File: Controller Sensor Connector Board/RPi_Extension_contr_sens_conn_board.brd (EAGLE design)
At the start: 100 x 100 mm, 39 parts, among them J1 22-27-2051-05, J2 22-27-2051-05, X17 53047-03, X18 53047-03, X19 53047-03, X20 53047-03, X21 53047-03, X22 53047-03, X23 53047-03, X24 53047-03, X25 53047-03, X26 53047-03, X27 53047-03, X28 53047-03, X29 53047-03, X30 53047-03, X31 53047-03, X32 53047-03

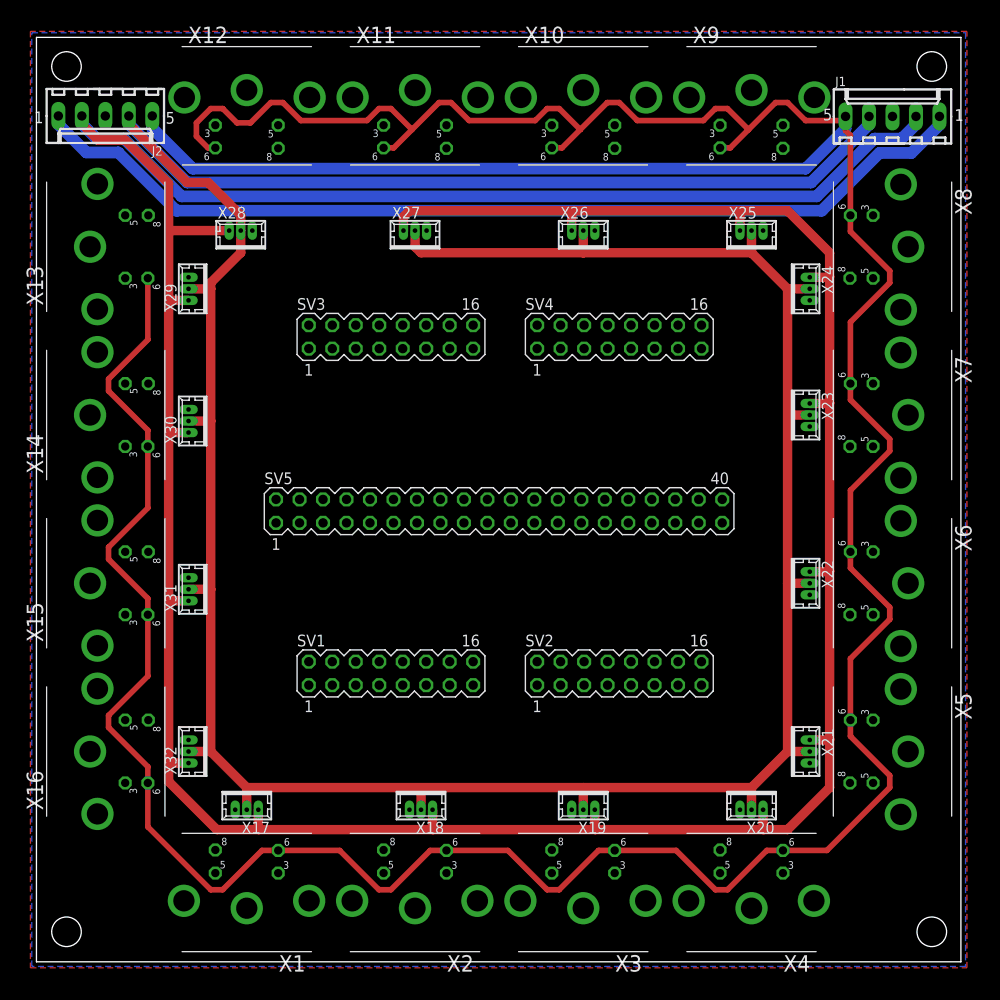
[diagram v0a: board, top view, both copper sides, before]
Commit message: added 40pin connector using 3pin 2row for each muscle
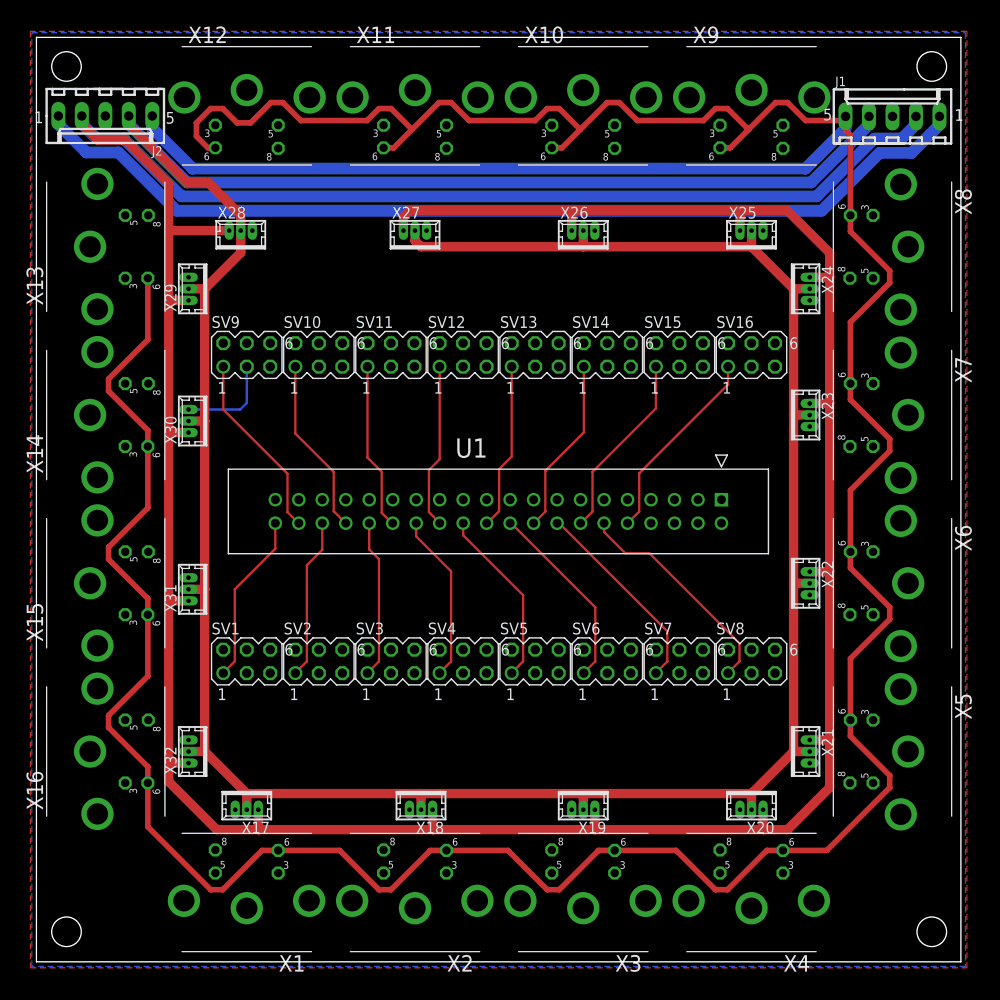
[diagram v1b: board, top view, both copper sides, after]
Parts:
- added SV10, SV11, SV12, SV13, SV14, SV15, SV16, SV6, SV7, SV8, SV9: (no value), con-lstb:MA03-2
- added U1: 5103309-8, AMP 5103309-8 40pin:TYCO_5103309-8
- SV1, SV2, SV3, SV4: device con-lstb:MA08-2 -> con-lstb:MA03-2
- SV5: device con-lstb:MA20-2 -> con-lstb:MA03-2
- moved SV4 39.0 mm to (46.1, 32.5)
- moved SV3 35.1 mm to (38.4, 32.5)
- moved SV2 32.5 mm to (30.6, 32.5)
- moved SV5 16.7 mm to (54.0, 32.5)
- moved SV1 15.7 mm to (22.8, 32.5)
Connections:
- removed net N$43: X30.1
- new net ADC_1: SV1.3
- new net ADC_10: SV10.3
- new net ADC_11: SV11.3
- new net ADC_12: SV12.3
- new net ADC_13: SV13.3
- new net ADC_14: SV14.3
- new net ADC_15: SV15.3
- new net ADC_16: SV16.3
- new net ADC_2: SV2.3
- new net ADC_3: SV3.3
- new net ADC_4: SV4.3
- new net ADC_5: SV5.3
- new net ADC_6: SV6.3
- new net ADC_7: SV7.3
- new net ADC_8: SV8.3
- new net ADC_9: SV9.3, X30.1
- new net DAC_1: SV1.1, U1.40
- new net DAC_10: SV10.1, U1.34
- new net DAC_11: SV11.1, U1.30
- new net DAC_12: SV12.1, U1.26
- new net DAC_13: SV13.1, U1.22
- new net DAC_14: SV14.1, U1.18
- new net DAC_15: SV15.1, U1.14
- new net DAC_16: SV16.1, U1.10
- new net DAC_2: SV2.1, U1.36
- new net DAC_3: SV3.1, U1.32
- new net DAC_4: SV4.1, U1.28
- new net DAC_5: SV5.1, U1.24
- new net DAC_6: SV6.1, U1.20
- new net DAC_7: SV7.1, U1.16
- new net DAC_8: SV8.1, U1.12
- new net DAC_9: SV9.1, U1.38
- new net N$100: X1.5
- new net N$101: X5.3
- new net N$102: X5.5
- new net N$103: X9.5
- new net N$104: X9.3
- new net N$105: X2.5
- new net N$106: X2.3
- new net N$107: X6.5
- new net N$108: X6.3
- new net N$109: X10.5
- new net N$11: X11.3
- new net N$110: X10.3
- new net N$111: X16.5
- new net N$112: X16.3
- new net N$12: X11.5
- new net N$14: X7.3
- new net N$15: X7.5
- new net N$17: X3.3
- new net N$18: X3.5
- new net N$2: X13.5
- new net N$20: X4.3
- new net N$21: X4.5
- new net N$23: X8.5
- new net N$24: X8.3
- new net N$26: X12.5
- new net N$27: X12.3
- new net N$3: X13.3
- new net N$5: X14.5
- new net N$6: X14.3
- new net N$67: SV1.6
- new net N$68: SV1.5
- new net N$69: SV5.5
- new net N$70: SV5.6
- new net N$71: SV2.6
- new net N$72: SV2.5
- new net N$73: SV6.6
- new net N$74: SV6.5
- new net N$75: SV9.6
- new net N$76: SV9.5
- new net N$77: SV13.6
- new net N$78: SV13.5
- new net N$79: SV10.6
- new net N$8: X15.3
- new net N$80: SV10.5
- new net N$81: SV14.5
- new net N$82: SV14.6
- new net N$83: SV15.5
- new net N$84: SV15.6
- new net N$85: SV16.6
- new net N$86: SV16.5
- new net N$87: SV12.5
- new net N$88: SV12.6
- new net N$89: SV11.6
- new net N$9: X15.5
- new net N$90: SV11.5
- new net N$91: SV8.5
- new net N$92: SV8.6
- new net N$93: SV4.5
- new net N$94: SV4.6
- new net N$95: SV3.5
- new net N$96: SV3.6
- new net N$97: SV7.5
- new net N$98: SV7.6
- new net N$99: X1.3
- net GND: now also SV1.2, SV1.4, SV10.2, SV10.4, SV11.2, SV11.4, SV12.2, SV12.4, SV13.2, SV13.4, SV14.2, SV14.4, SV15.2, SV15.4, SV16.2, SV16.4, SV2.2, SV2.4, SV3.2, SV3.4, SV4.2, SV4.4, SV5.2, SV5.4, SV6.2, SV6.4, SV7.2, SV7.4, SV8.2, SV8.4, SV9.2, SV9.4, U1.1, U1.11, U1.13, U1.15, U1.17, U1.19, U1.21, U1.23, U1.25, U1.27, U1.29, U1.3, U1.31, U1.33, U1.35, U1.37, U1.39, U1.5, U1.7, U1.9
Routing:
- net DAC_8: track 0.00 -> 24.3 mm
- net DAC_7: track 0.00 -> 21.8 mm
- net DAC_16: track 0.00 -> 21.4 mm
- net DAC_6: track 0.00 -> 20.6 mm
- net DAC_9: track 0.00 -> 20.3 mm
- net DAC_15: track 0.00 -> 20.3 mm
- net DAC_5: track 0.00 -> 19.4 mm
- net DAC_10: track 0.00 -> 19.2 mm
- net DAC_14: track 0.00 -> 19.2 mm
- net DAC_1: track 0.00 -> 18.6 mm
- net DAC_4: track 0.00 -> 18.3 mm
- net DAC_11: track 0.00 -> 18.1 mm
- net DAC_13: track 0.00 -> 18.1 mm
- net DAC_12: track 0.00 -> 17.9 mm
- net DAC_2: track 0.00 -> 17.4 mm
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
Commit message: finished first half of connector board
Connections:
- net N$67 renamed LC_P_1
- net N$68 renamed LC_N_1
- removed net N$103: X9.5
- removed net N$104: X9.3
- removed net N$109: X10.5
- removed net N$11: X11.3
- removed net N$110: X10.3
- removed net N$12: X11.5
- removed net N$13: X24.1
- removed net N$14: X7.3
- removed net N$15: X7.5
- removed net N$16: X23.1
- removed net N$2: X13.5
- removed net N$23: X8.5
- removed net N$24: X8.3
- removed net N$25: X25.1
- removed net N$26: X12.5
- removed net N$27: X12.3
- removed net N$28: X26.1
- removed net N$3: X13.3
- removed net N$31: X27.1
- removed net N$34: X28.1
- removed net N$46: X29.1
- removed net N$5: X14.5
- removed net N$6: X14.3
- removed net N$75: SV9.6
- removed net N$76: SV9.5
- removed net N$77: SV13.6
- removed net N$78: SV13.5
- removed net N$79: SV10.6
- removed net N$80: SV10.5
- removed net N$81: SV14.5
- removed net N$82: SV14.6
- removed net N$83: SV15.5
- removed net N$84: SV15.6
- removed net N$85: SV16.6
- removed net N$86: SV16.5
- removed net N$87: SV12.5
- removed net N$88: SV12.6
- removed net N$89: SV11.6
- removed net N$90: SV11.5
- new net LC_N_10: SV10.5, X13.3
- new net LC_N_11: SV11.5, X12.3
- new net LC_N_12: SV12.5, X11.3
- new net LC_N_13: SV13.5, X10.3
- new net LC_N_14: SV14.5, X9.3
- new net LC_N_15: SV15.5, X8.3
- new net LC_N_16: SV16.5, X7.3
- new net LC_N_9: SV9.5, X14.3
- new net LC_P_10: SV10.6, X13.5
- new net LC_P_11: SV11.6, X12.5
- new net LC_P_12: SV12.6, X11.5
- new net LC_P_13: SV13.6, X10.5
- new net LC_P_14: SV14.6, X9.5
- new net LC_P_15: SV15.6, X8.5
- new net LC_P_16: SV16.6, X7.5
- new net LC_P_9: SV9.6, X14.5
- net ADC_10: now also X29.1
- net ADC_11: now also X28.1
- net ADC_12: now also X27.1
- net ADC_13: now also X26.1
- net ADC_14: now also X25.1
- net ADC_15: now also X24.1
- net ADC_16: now also X23.1
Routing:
- net LC_P_14: track 0.00 -> 92.1 mm
- net LC_N_14: track 0.00 -> 88.8 mm
- net LC_P_13: track 0.00 -> 69.2 mm
- net LC_N_13: track 0.00 -> 66.9 mm
- net LC_P_12: track 0.00 -> 46.3 mm
- net LC_N_12: track 0.00 -> 42.8 mm
- net LC_N_11: track 0.00 -> 37.3 mm
- net LC_P_9: track 0.00 -> 36.1 mm
- net LC_P_11: track 0.00 -> 33.6 mm
- net LC_N_15: track 0.00 -> 33.5 mm
- net LC_P_10: track 0.00 -> 31.6 mm
- net LC_N_10: track 0.00 -> 29.8 mm
- net ADC_14: track 0.00 -> 25.5 mm
- net ADC_11: track 0.00 -> 22.6 mm
- net LC_P_15: track 0.00 -> 22.3 mm
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
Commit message: finished second half of connector board
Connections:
- removed net N$1: X17.1
- removed net N$10: X20.1
- removed net N$100: X1.5
- removed net N$101: X5.3
- removed net N$102: X5.5
- removed net N$105: X2.5
- removed net N$106: X2.3
- removed net N$107: X6.5
- removed net N$108: X6.3
- removed net N$111: X16.5
- removed net N$112: X16.3
- removed net N$17: X3.3
- removed net N$18: X3.5
- removed net N$19: X22.1
- removed net N$20: X4.3
- removed net N$21: X4.5
- removed net N$22: X21.1
- removed net N$37: X32.1
- removed net N$4: X18.1
- removed net N$40: X31.1
- removed net N$69: SV5.5
- removed net N$7: X19.1
- removed net N$70: SV5.6
- removed net N$71: SV2.6
- removed net N$72: SV2.5
- removed net N$73: SV6.6
- removed net N$74: SV6.5
- removed net N$8: X15.3
- removed net N$9: X15.5
- removed net N$91: SV8.5
- removed net N$92: SV8.6
- removed net N$93: SV4.5
- removed net N$94: SV4.6
- removed net N$95: SV3.5
- removed net N$96: SV3.6
- removed net N$97: SV7.5
- removed net N$98: SV7.6
- removed net N$99: X1.3
- new net LC_N_2: SV2.5, X16.3
- new net LC_N_3: SV3.5, X1.3
- new net LC_N_4: SV4.5, X2.3
- new net LC_N_5: SV5.5, X3.3
- new net LC_N_6: SV6.5, X4.3
- new net LC_N_7: SV7.5, X5.3
- new net LC_N_8: SV8.5, X6.3
- new net LC_P_2: SV2.6, X16.5
- new net LC_P_3: SV3.6, X1.5
- new net LC_P_4: SV4.6, X2.5
- new net LC_P_5: SV5.6, X3.5
- new net LC_P_6: SV6.6, X4.5
- new net LC_P_7: SV7.6, X5.5
- new net LC_P_8: SV8.6, X6.5
- net ADC_1: now also X31.1
- net ADC_2: now also X32.1
- net ADC_3: now also X17.1
- net ADC_4: now also X18.1
- net ADC_5: now also X19.1
- net ADC_6: now also X20.1
- net ADC_7: now also X21.1
- net ADC_8: now also X22.1
- net LC_N_1: now also X15.3
- net LC_P_1: now also X15.5
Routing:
- net LC_P_6: track 0.00 -> 39.3 mm
- net LC_P_2: track 0.00 -> 35.9 mm
- net LC_P_3: track 0.00 -> 33.9 mm
- net LC_N_6: track 0.00 -> 33.7 mm
- net LC_P_5: track 0.00 -> 32.1 mm
- net LC_N_2: track 0.00 -> 31.1 mm
- net LC_P_4: track 0.00 -> 29.9 mm
- net LC_P_7: track 0.00 -> 29.5 mm
- net LC_P_1: track 0.00 -> 28.4 mm
- net LC_N_3: track 0.00 -> 27.8 mm
- net LC_N_5: track 0.00 -> 25.8 mm
- net ADC_3: track 0.00 -> 25.6 mm
- net LC_N_4: track 0.00 -> 23.4 mm
- net ADC_6: track 0.00 -> 22.8 mm
- net LC_N_8: track 0.00 -> 22.7 mm
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
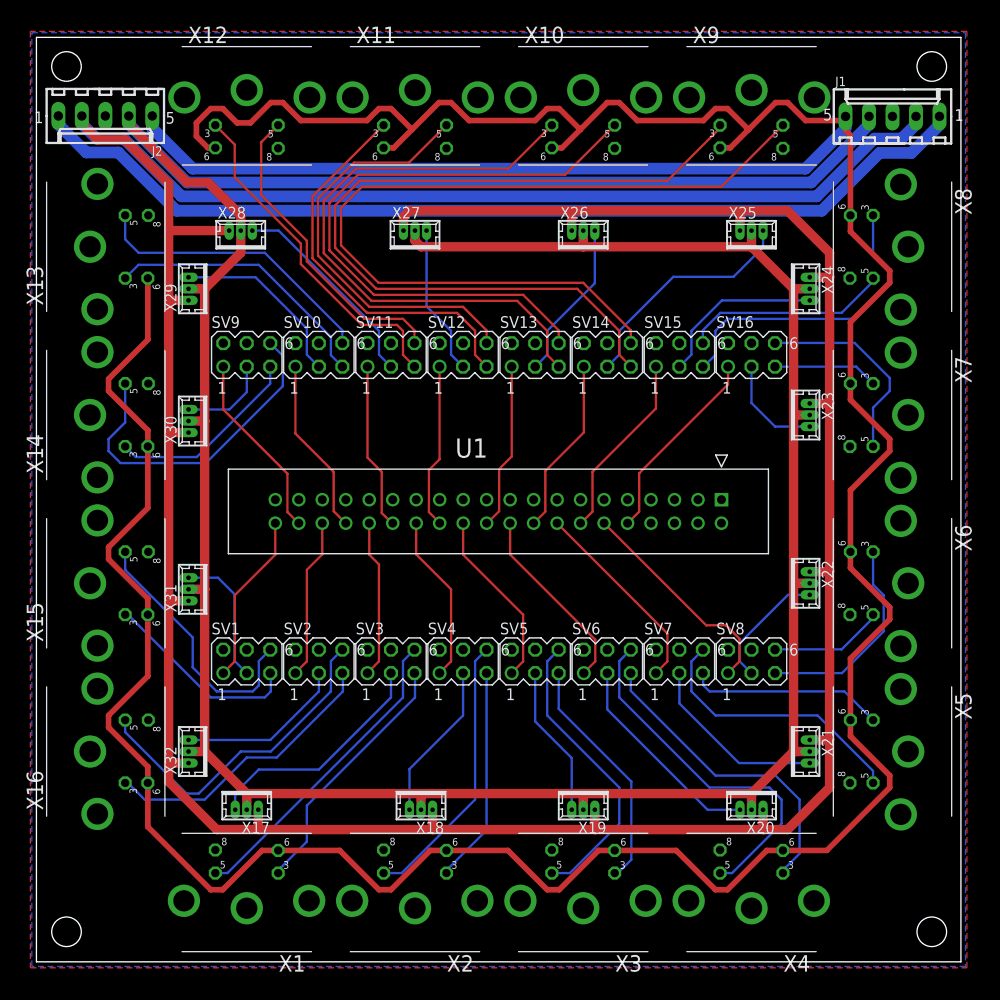
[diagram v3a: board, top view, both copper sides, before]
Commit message: adjusted silkscreen
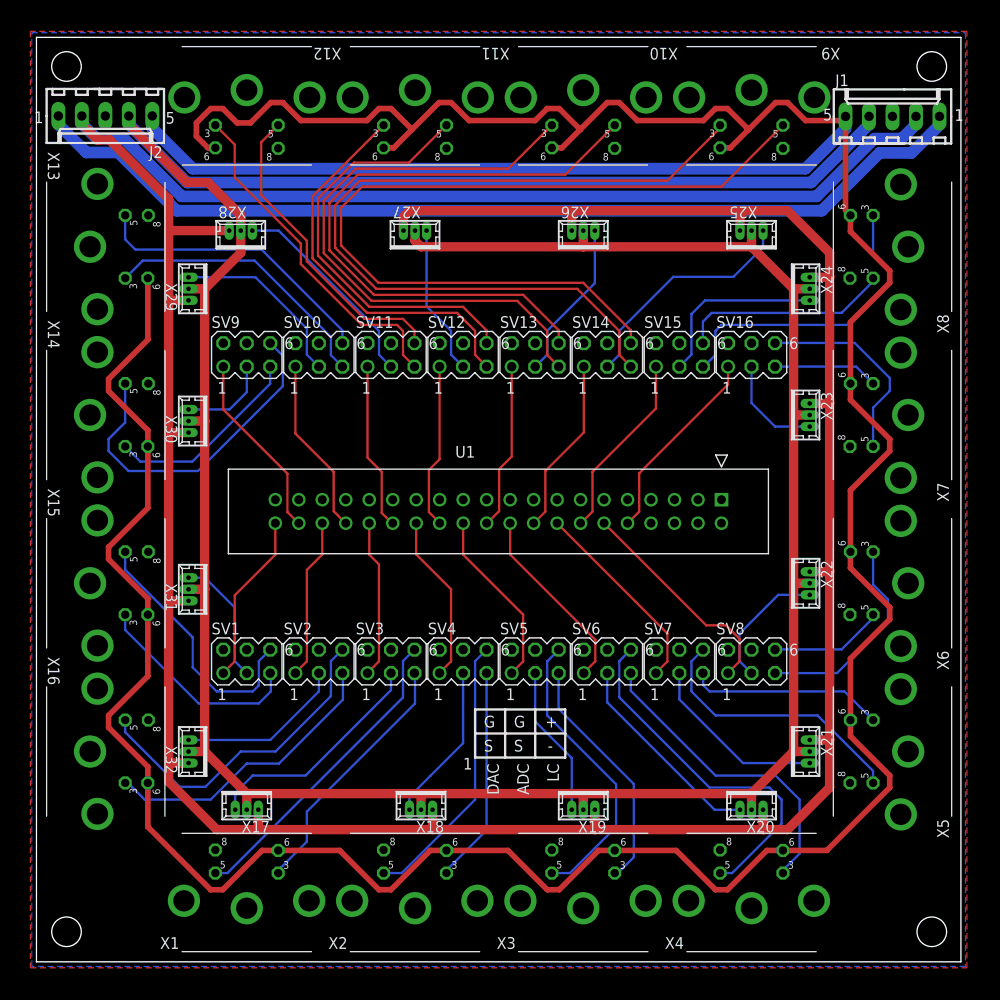
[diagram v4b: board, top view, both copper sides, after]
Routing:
- net LC_N_1: track 21.7 -> 23.2 mm
- net ADC_15: track 18.6 -> 19.6 mm
- net +12V: track 396.2 -> 395.2 mm
- net ADC_1: track 14.8 -> 14.0 mm
- net LC_P_9: track 36.1 -> 36.8 mm
- net ADC_8: track 13.5 -> 14.1 mm
- net LC_P_15: track 22.3 -> 22.9 mm
- net LC_N_2: track 31.1 -> 31.7 mm
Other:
- board text added: "+"
- board text added: "-"
- board text added: "1"
- board text added: "ADC"
- board text added: "DAC"
- board text added: "G"
- board text added: "LC"
- board text added: "S"

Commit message: changed dac header to 34pin
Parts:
- U1: value 5103309-8 -> 5103309-7; device AMP 5103309-8 40pin:TYCO_5103309-8 -> AMP 5103309-7 34pin:TYCO_5103309-7
- moved U1 43.7 mm to (30.6, 50.7), turned to 180 degrees
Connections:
- net DAC_1: now also U1.1; no longer U1.40
- net DAC_10: now also U1.7; no longer U1.34
- net DAC_11: now also U1.11; no longer U1.30
- net DAC_12: now also U1.15; no longer U1.26
- net DAC_13: now also U1.19; no longer U1.22
- net DAC_14: now also U1.23; no longer U1.18
- net DAC_15: now also U1.27; no longer U1.14
- net DAC_16: now also U1.31; no longer U1.10
- net DAC_2: now also U1.5; no longer U1.36
- net DAC_3: now also U1.9; no longer U1.32
- net DAC_4: now also U1.13; no longer U1.28
- net DAC_5: now also U1.17; no longer U1.24
- net DAC_6: now also U1.21; no longer U1.20
- net DAC_7: now also U1.25; no longer U1.16
- net DAC_8: now also U1.29; no longer U1.12
- net DAC_9: now also U1.3; no longer U1.38
- net GND: now also U1.10, U1.12, U1.14, U1.16, U1.18, U1.2, U1.20, U1.22, U1.24, U1.26, U1.28, U1.30, U1.32, U1.34, U1.4, U1.6, U1.8; no longer U1.1, U1.11, U1.13, U1.15, U1.17, U1.19, U1.21, U1.23, U1.25, U1.27, U1.29, U1.3, U1.31, U1.33, U1.35, U1.37, U1.39, U1.5, U1.7, U1.9
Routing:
- net DAC_15: track 20.3 -> 17.6 mm
- net DAC_16: track 21.4 -> 18.8 mm
- net DAC_2: track 17.4 -> 20.1 mm
- net DAC_1: track 18.6 -> 21.2 mm
- net DAC_8: track 24.1 -> 21.6 mm
- net DAC_3: track 17.2 -> 19.0 mm
- net DAC_14: track 19.2 -> 17.6 mm
- net DAC_7: track 21.7 -> 20.4 mm
- net DAC_6: track 20.5 -> 19.3 mm
- net DAC_5: track 19.4 -> 18.2 mm
- net DAC_10: track 19.2 -> 20.4 mm
- net DAC_9: track 20.3 -> 21.6 mm
- net DAC_11: track 18.1 -> 19.3 mm
- net DAC_13: track 18.1 -> 17.0 mm
